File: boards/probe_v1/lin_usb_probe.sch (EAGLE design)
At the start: 31 parts, among them J1 AVR_SPI_PRG_6NS, J2 12146734, U1 ATtiny167, U2 MCP2025, U3 MC17XSF500

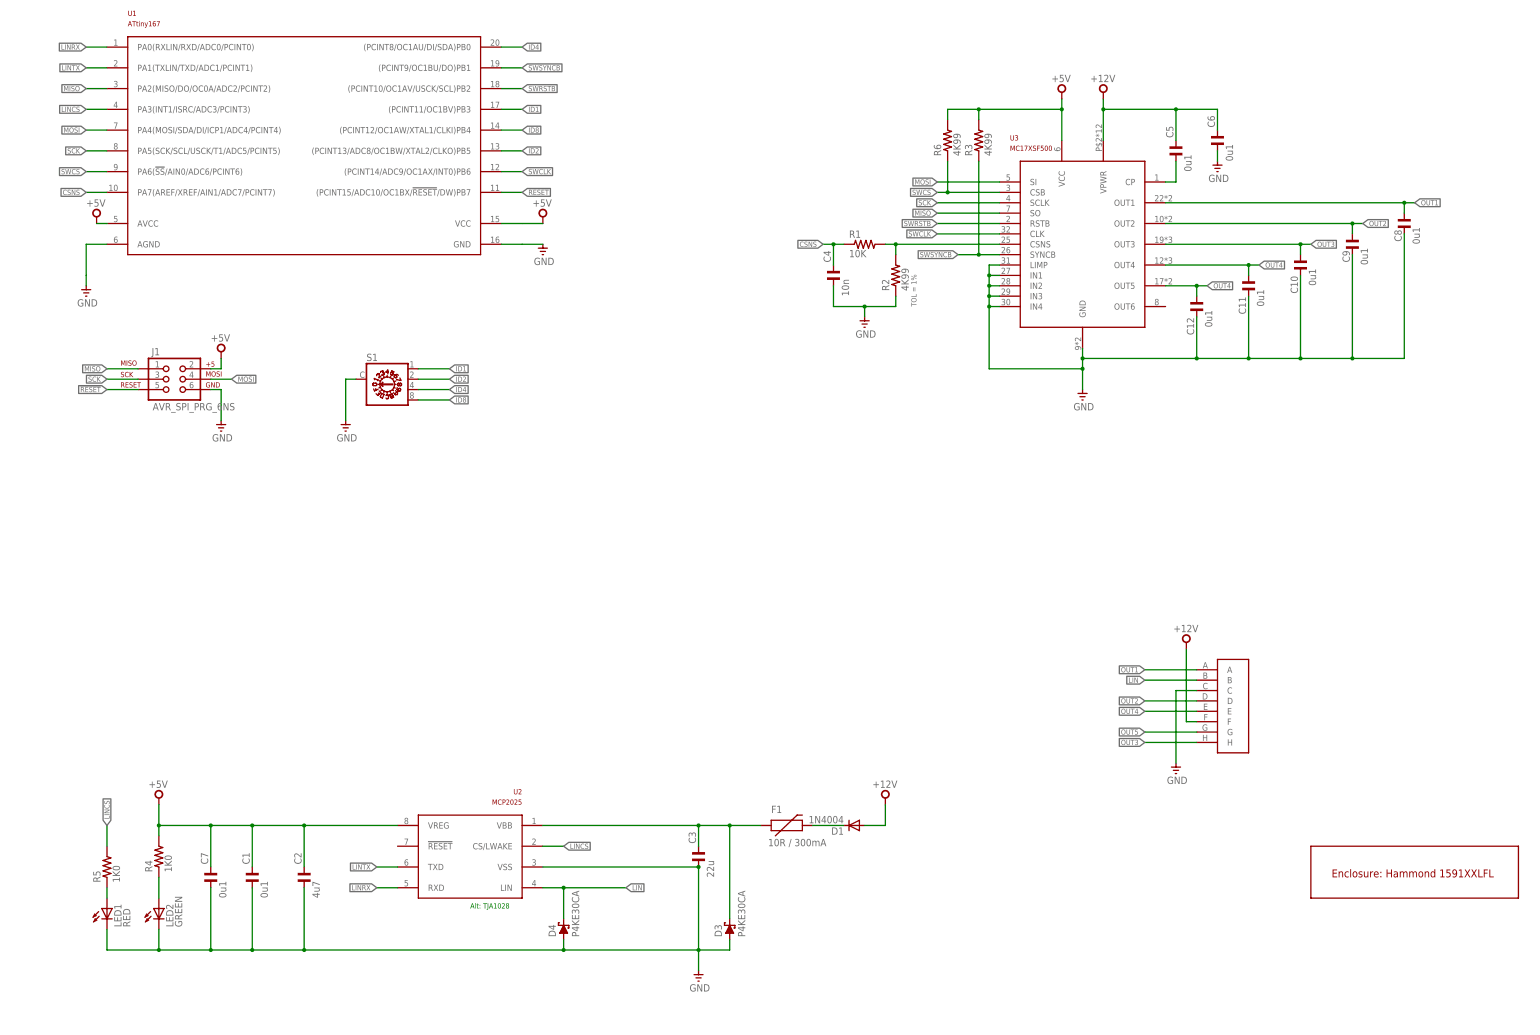
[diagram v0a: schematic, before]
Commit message: Update to current sample boards
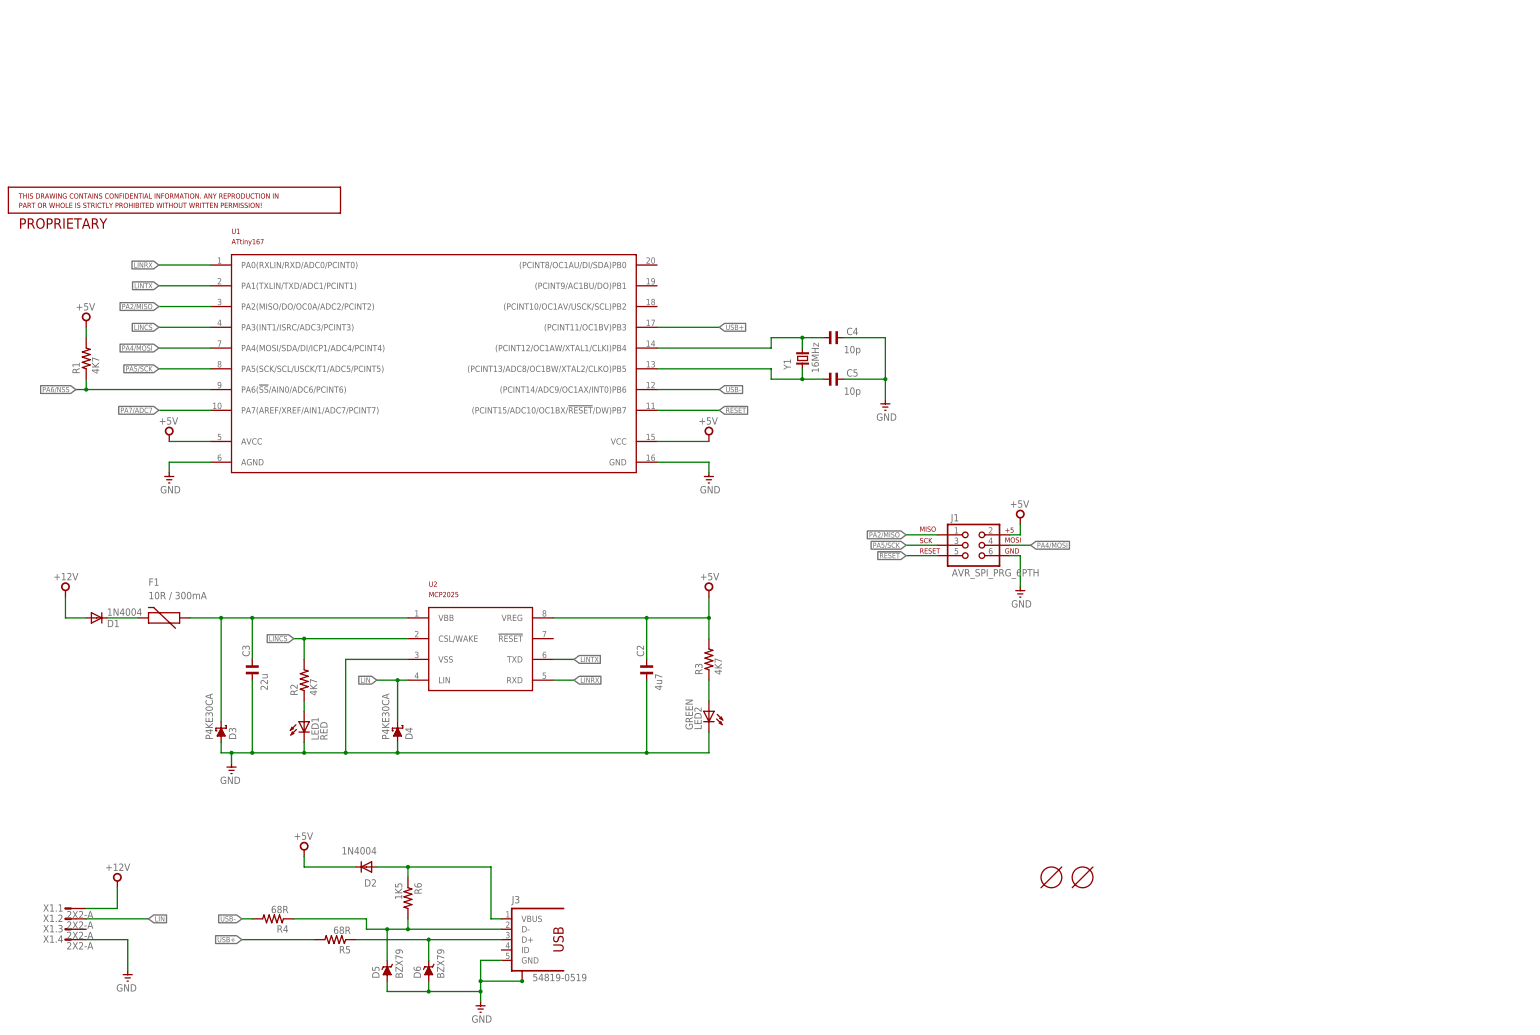
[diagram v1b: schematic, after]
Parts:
- removed C1, C6, C7: 0u1, custom:C-EU050-024X044
- removed C10, C11, C12, C8, C9: 0u1, custom:C-EUC0603K
- removed J2: 12146734, custom:12146734
- removed S1: (no value), custom:P103
- removed U3: MC17XSF500, custom:MC17XSF500
- added D2: 1N4004, custom:1N4004
- added D5, D6: BZX79, custom:BZX79
- added J3: 54819-0519, custom:54819-0519
- added U$2: MOUNT-HOLE3.1MM, custom:MOUNT-HOLE3.1MM
- added X1: 2X2-A, custom:2X2-A
- added Y1: 16MHz, custom:CRYTALHC49S
- C2: PARTNO FK28X5R0J475K -> GRM21BR71A475KA73K
- C3: PARTNO FK22X5R1E226M -> C2012X5R1V226M125AC
- C4: value 10n -> 10p; PARTNO FK18X7R1H103K -> (none)
- C5: value 0u1 -> 10p; device custom:C-EU050-024X044 -> custom:C-EU025-024X044; PARTNO FK28X7R1H104K -> (none)
- D3, D4: device custom:P4KEXX -> custom:SCHOTTKY-DIODEDO41-10
- F1: PARTNO CMF-RL10-0 -> 600R150-RBZR
- J1: value AVR_SPI_PRG_6NS -> AVR_SPI_PRG_6PTH; device custom:AVR_SPI_PRG_6NS -> custom:AVR_SPI_PRG_6PTH
- R1: value 10K -> 4K7; PARTNO CF14JT10K0 -> ERJ-6GEYJ472V
- R2: value 4K99 -> 4K7; PARTNO MFR-25FBF52-4K99 -> ERJ-6GEYJ472V; TOL 1% -> (none)
- R3: value 4K99 -> 4K7; PARTNO MFR-25FBF52-4K99 -> ERJ-6GEYJ472V
- R4, R5: value 1K0 -> 68R; PARTNO CF14JT1K00 -> ERJ-6GEYJ472V
- R6: value 4K99 -> 1K5; PARTNO MFR-25FBF52-4K99 -> ERJ-6GEYJ472V
- U$1: value 1591XXLFL -> MOUNT-HOLE3.1MM; device custom:1591XXLFL -> custom:MOUNT-HOLE3.1MM; PARTNO 1591XXLFLBK -> (none)
- U1: device custom:ATTINY167 -> custom:ATTINY16720X; PARTNO ATTINY167-SU -> ATTINY167-A15XZ
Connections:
- removed net CSNS: C4.1, R1.1, U1.PA7(AREF/XREF/AIN1/ADC7/PCINT7)
- removed net ID1: S1.1, U1.(PCINT11/OC1BV)PB3
- removed net ID2: S1.2, U1.(PCINT13/ADC8/OC1BW/XTAL2/CLKO)PB5
- removed net ID4: S1.4, U1.(PCINT8/OC1AU/DI/SDA)PB0
- removed net ID8: S1.8, U1.(PCINT12/OC1AW/XTAL1/CLKI)PB4
- removed net MISO: J1.1, U1.PA2(MISO/DO/OC0A/ADC2/PCINT2), U3.SO
- removed net MOSI: J1.4, U1.PA4(MOSI/SDA/DI/ICP1/ADC4/PCINT4), U3.SI
- removed net OUT1: C8.1, J2.A, U3.OUT1
- removed net OUT2: C9.1, J2.D, U3.OUT2
- removed net OUT3: C10.1, J2.H, U3.OUT3
- removed net OUT4: C11.1, J2.E, U3.OUT4
- removed net OUT5: C12.1, J2.G, U3.OUT5
- removed net SCK: J1.3, U1.PA5(SCK/SCL/USCK/T1/ADC5/PCINT5), U3.SCLK
- removed net SWCLK: U1.(PCINT14/ADC9/OC1AX/INT0)PB6, U3.CLK
- removed net SWCS: R6.1, U1.PA6(!SS!/AIN0/ADC6/PCINT6), U3.CSB
- removed net SWRSTB: U1.(PCINT10/OC1AV/USCK/SCL)PB2, U3.RSTB
- removed net SWSYNCB: R3.1, U1.(PCINT9/OC1BU/DO)PB1, U3.SYNCB
- new net N$7: D5.C, J3.D-, R4.1, R6.2
- new net N$8: D2.A, J3.VBUS, R6.1
- new net N$9: C5.2, U1.(PCINT13/ADC8/OC1BW/XTAL2/CLKO)PB5, Y1.1
- new net PA2/MISO: J1.1, U1.PA2(MISO/DO/OC0A/ADC2/PCINT2)
- new net PA4/MOSI: J1.4, U1.PA4(MOSI/SDA/DI/ICP1/ADC4/PCINT4)
- new net PA5/SCK: J1.3, U1.PA5(SCK/SCL/USCK/T1/ADC5/PCINT5)
- new net PA6/NSS: R1.1, U1.PA6(!SS!/AIN0/ADC6/PCINT6)
- new net PA7/ADC7: U1.PA7(AREF/XREF/AIN1/ADC7/PCINT7)
- new net USB+: R5.2, U1.(PCINT11/OC1BV)PB3
- new net USB-: R4.2, U1.(PCINT14/ADC9/OC1AX/INT0)PB6
- net +12V: now also X1.1.S; no longer C5.1, C6.1, J2.F, U3.VPWR
- net +5V: now also D2.C, R1.2; no longer C1.1, C7.1, R4.2, R6.2, U3.VCC
- net GND: now also C4.1, C5.1, D5.A, D6.A, J3.GND, J3.S1, J3.S2, X1.4.S; no longer C1.2, C10.2, C11.2, C12.2, C4.2, C6.2, C7.2, C8.2, C9.2, J2.C, R2.1, S1.C, U3.GND, U3.IN1, U3.IN2, U3.IN3, U3.IN4, U3.LIMP
- net LIN: now also X1.2.S; no longer J2.B
- net LINCS: now also R2.2, U2.CSL/WAKE; no longer R5.2, U2.CS/LWAKE
- net N$1: now also C4.2, U1.(PCINT12/OC1AW/XTAL1/CLKI)PB4, Y1.2; no longer C5.2, U3.CP
- net N$3: now also R2.1; no longer R5.1
- net N$4: now also R3.1; no longer R4.1
- net N$6: now also D6.C, J3.D+, R5.1; no longer R1.2, R2.2, U3.CSNS
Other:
- note removed: "Alt: TJA1028"
- moved on the sheet: C2, C3, C4, C5, D1, F1, J1, LED1, LED2, R1, R2, R3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
